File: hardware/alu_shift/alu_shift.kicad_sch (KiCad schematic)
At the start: 3 parts, among them J1 Conn_02x17_Odd_Even, U1 74HC00

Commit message: added LED indicators for ALU shift module
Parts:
- added D10, D11, D12, D13, D14, D15, D16, D17, D18, D19, D20, D21, D22, D23, D24, D25, D26, D27, D28, D8, D9: LED, LED_SMD:LED_0603_1608Metric_Pad1.05x0.95mm_HandSolder, symbol Device:LED
- added Q15, Q16, Q17, Q18, Q19, Q20, Q21, Q22, Q23, Q24, Q25, Q26, Q27, Q28, Q29, Q30, Q31, Q32, Q33, Q34, Q35: IRLML6244, Package_TO_SOT_SMD:SOT-23_Handsoldering, symbol Transistor_FET:IRLML6244
- added R22, R23, R24, R25, R26, R27, R28, R29, R30, R31, R32, R33, R34, R35, R36, R37, R38, R39, R40, R41, R42: 1000, Resistor_SMD:R_0603_1608Metric_Pad0.98x0.95mm_HandSolder, symbol Device:R
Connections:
- net +5V: now also Q15.3 (D), Q16.3 (D), Q17.3 (D), Q18.3 (D), Q19.3 (D), Q20.3 (D), Q21.3 (D), Q22.3 (D), Q23.3 (D), Q24.3 (D), Q25.3 (D), Q26.3 (D), Q27.3 (D), Q28.3 (D), Q29.3 (D), Q30.3 (D), Q31.3 (D), Q32.3 (D), Q33.3 (D), Q34.3 (D), Q35.3 (D)
- net A0: now also Q15.1 (G)
- net A1: now also Q16.1 (G)
- net A2: now also Q17.1 (G)
- net A3: now also Q18.1 (G)
- net A4: now also Q19.1 (G)
- net A5: now also Q20.1 (G)
- net A6: now also Q21.1 (G)
- net A7: now also Q22.1 (G)
- net BY0: now also Q31.1 (G)
- net BY1: now also Q32.1 (G)
- net BY2: now also Q33.1 (G)
- net DIR: now also Q35.1 (G); no longer U1.10, U1.4, U1.9
- net GND: now also R22.2, R23.2, R24.2, R25.2, R26.2, R27.2, R28.2, R29.2, R30.2, R31.2, R32.2, R33.2, R34.2, R35.2, R36.2, R37.2, R38.2, R39.2, R40.2, R41.2, R42.2
- net RES0: now also D16.2 (A), Q23.2 (S)
- net RES1: now also D17.2 (A), Q24.2 (S)
- net RES2: now also D18.2 (A), Q25.2 (S)
- net RES3: now also D19.2 (A), Q26.2 (S)
- net RES4: now also D20.2 (A), Q27.2 (S)
- net RES5: now also D21.2 (A), Q28.2 (S)
- net RES6: now also D22.2 (A), Q29.2 (S)
- net RES7: now also D23.2 (A), Q30.2 (S)
- net SOB: now also D27.2 (A), Q34.2 (S); no longer U1.11
- new net: D12.1 (K), R26.1
- new net: D11.1 (K), R25.1
- new net: D17.1 (K), R31.1
- new net: D8.1 (K), R22.1
- new net: D20.1 (K), R34.1
- new net: D19.1 (K), R33.1
- new net: D23.1 (K), R37.1
- new net: D25.1 (K), R39.1
- new net: Q34.1 (G), U1.11
- new net: D13.1 (K), R27.1
- new net: D27.1 (K), R41.1
- new net: D22.1 (K), R36.1
- new net: D15.1 (K), R29.1
- new net: D24.1 (K), R38.1
- new net: D28.1 (K), R42.1
- new net: D16.1 (K), R30.1
- new net: D10.1 (K), R24.1
- new net: D14.1 (K), R28.1
- new net: D21.1 (K), R35.1
- new net: D18.1 (K), R32.1
- new net: D9.1 (K), R23.1
- new net: D26.1 (K), R40.1
- new net MuxDirection/OUT0: Q23.1 (G)
- new net MuxDirection/OUT1: Q24.1 (G)
- new net MuxDirection/OUT2: Q25.1 (G)
- new net MuxDirection/OUT3: Q26.1 (G)
- new net MuxDirection/OUT4: Q27.1 (G)
- new net MuxDirection/OUT5: Q28.1 (G)
- new net MuxDirection/OUT6: Q29.1 (G)
- new net MuxDirection/OUT7: Q30.1 (G)
- new net MuxDirection/SEL: D28.2 (A), Q35.2 (S), U1.10, U1.4, U1.9
- new net MuxLeft1/A0: D8.2 (A), Q15.2 (S)
- new net MuxLeft1/A1: D9.2 (A), Q16.2 (S)
- new net MuxLeft1/A2: D10.2 (A), Q17.2 (S)
- new net MuxLeft1/A3: D11.2 (A), Q18.2 (S)
- new net MuxLeft1/A4: D12.2 (A), Q19.2 (S)
- new net MuxLeft1/A5: D13.2 (A), Q20.2 (S)
- new net MuxLeft1/A6: D14.2 (A), Q21.2 (S)
- new net MuxLeft1/A7: D15.2 (A), Q22.2 (S)
- new net MuxLeft1/SEL: D24.2 (A), Q31.2 (S)
- new net MuxLeft2/SEL: D25.2 (A), Q32.2 (S)
- new net MuxLeft4/SEL: D26.2 (A), Q33.2 (S)
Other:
- moved on the sheet: U1A, U1B, U1C, U1D

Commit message: added 8 bit mux pcb, started work on ALU shifter
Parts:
- Q1: renamed from Q15; footprint Package_TO_SOT_SMD:SOT-23_Handsoldering -> Package_TO_SOT_SMD:SOT-23-3
- Q10: renamed from Q31; footprint Package_TO_SOT_SMD:SOT-23_Handsoldering -> Package_TO_SOT_SMD:SOT-23-3
- Q11: renamed from Q35; footprint Package_TO_SOT_SMD:SOT-23_Handsoldering -> Package_TO_SOT_SMD:SOT-23-3
- Q12: renamed from Q32; footprint Package_TO_SOT_SMD:SOT-23_Handsoldering -> Package_TO_SOT_SMD:SOT-23-3
- Q13: renamed from Q33; footprint Package_TO_SOT_SMD:SOT-23_Handsoldering -> Package_TO_SOT_SMD:SOT-23-3
- Q14: renamed from Q23; footprint Package_TO_SOT_SMD:SOT-23_Handsoldering -> Package_TO_SOT_SMD:SOT-23-3
- Q15: renamed from Q24; footprint Package_TO_SOT_SMD:SOT-23_Handsoldering -> Package_TO_SOT_SMD:SOT-23-3
- Q16: renamed from Q25; footprint Package_TO_SOT_SMD:SOT-23_Handsoldering -> Package_TO_SOT_SMD:SOT-23-3
- Q17: renamed from Q26; footprint Package_TO_SOT_SMD:SOT-23_Handsoldering -> Package_TO_SOT_SMD:SOT-23-3
- Q18: renamed from Q27; footprint Package_TO_SOT_SMD:SOT-23_Handsoldering -> Package_TO_SOT_SMD:SOT-23-3
- Q19: renamed from Q28; footprint Package_TO_SOT_SMD:SOT-23_Handsoldering -> Package_TO_SOT_SMD:SOT-23-3
- Q2: renamed from Q16; footprint Package_TO_SOT_SMD:SOT-23_Handsoldering -> Package_TO_SOT_SMD:SOT-23-3
- Q20: renamed from Q29; footprint Package_TO_SOT_SMD:SOT-23_Handsoldering -> Package_TO_SOT_SMD:SOT-23-3
- Q21: renamed from Q30; footprint Package_TO_SOT_SMD:SOT-23_Handsoldering -> Package_TO_SOT_SMD:SOT-23-3
- Q3: renamed from Q17; footprint Package_TO_SOT_SMD:SOT-23_Handsoldering -> Package_TO_SOT_SMD:SOT-23-3
- Q4: renamed from Q18; footprint Package_TO_SOT_SMD:SOT-23_Handsoldering -> Package_TO_SOT_SMD:SOT-23-3
- Q5: renamed from Q19; footprint Package_TO_SOT_SMD:SOT-23_Handsoldering -> Package_TO_SOT_SMD:SOT-23-3
- Q6: renamed from Q20; footprint Package_TO_SOT_SMD:SOT-23_Handsoldering -> Package_TO_SOT_SMD:SOT-23-3
- Q7: renamed from Q21; footprint Package_TO_SOT_SMD:SOT-23_Handsoldering -> Package_TO_SOT_SMD:SOT-23-3
- Q8: renamed from Q22; footprint Package_TO_SOT_SMD:SOT-23_Handsoldering -> Package_TO_SOT_SMD:SOT-23-3
- Q9: renamed from Q34; footprint Package_TO_SOT_SMD:SOT-23_Handsoldering -> Package_TO_SOT_SMD:SOT-23-3
- renumbered D8 to D1, D24 to D10, D28 to D11, D25 to D12, D26 to D13, D16 to D14, D17 to D15, D18 to D16, D19 to D17, D20 to D18, D21 to D19, D9 to D2, D22 to D20, D23 to D21, D10 to D3, D11 to D4, D12 to D5, D13 to D6, D14 to D7, D15 to D8, D27 to D9, R22 to R1, R38 to R10, R42 to R11, R39 to R12, R40 to R13, R30 to R14, R31 to R15, R32 to R16, R33 to R17, R34 to R18, R35 to R19, R23 to R2, R36 to R20, R37 to R21, R24 to R3, R25 to R4, R26 to R5, R27 to R6, R28 to R7, R29 to R8, R41 to R9
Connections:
- net MuxDirection/OUT0 renamed MuxResult/RES0
- net MuxDirection/OUT1 renamed MuxResult/RES1
- net MuxDirection/OUT2 renamed MuxResult/RES2
- net MuxDirection/OUT3 renamed MuxResult/RES3
- net MuxDirection/OUT4 renamed MuxResult/RES4
- net MuxDirection/OUT5 renamed MuxResult/RES5
- net MuxDirection/OUT6 renamed MuxResult/RES6
- net MuxDirection/OUT7 renamed MuxResult/RES7
- net MuxDirection/SEL renamed MuxResult/SEL
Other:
- removed sheet MuxDirection
- added sheet MuxResult (mux.kicad_sch)
- sheet MuxLeft1 ports: added RES0, RES1, RES2, RES3, RES4, RES5, RES6, RES7; removed OUT0, OUT1, OUT2, OUT3, OUT4, OUT5, OUT6, OUT7
- sheet MuxLeft2 ports: added RES0, RES1, RES2, RES3, RES4, RES5, RES6, RES7; removed OUT0, OUT1, OUT2, OUT3, OUT4, OUT5, OUT6, OUT7
- sheet MuxLeft4 ports: added RES0, RES1, RES2, RES3, RES4, RES5, RES6, RES7; removed OUT0, OUT1, OUT2, OUT3, OUT4, OUT5, OUT6, OUT7
- sheet MuxRight1 ports: added RES0, RES1, RES2, RES3, RES4, RES5, RES6, RES7; removed OUT0, OUT1, OUT2, OUT3, OUT4, OUT5, OUT6, OUT7
- sheet MuxRight2 ports: added RES0, RES1, RES2, RES3, RES4, RES5, RES6, RES7; removed OUT0, OUT1, OUT2, OUT3, OUT4, OUT5, OUT6, OUT7
- sheet MuxRight4 ports: added RES0, RES1, RES2, RES3, RES4, RES5, RES6, RES7; removed OUT0, OUT1, OUT2, OUT3, OUT4, OUT5, OUT6, OUT7

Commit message: finished ALU Shift module, all ALU modules completed
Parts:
- added C12, C2, C3: 10uF, Capacitor_SMD:C_0603_1608Metric_Pad1.08x0.95mm_HandSolder, symbol Device:C
- added H1, H2, H3, H4: MountingHole_Pad, MountingHole:MountingHole_2.2mm_M2_Pad, symbol Mechanical:MountingHole_Pad
- added TP1, TP10, TP11, TP12, TP13, TP14, TP15, TP16, TP17, TP18, TP19, TP2, TP20, TP21, TP22, TP23, TP24, TP25, TP26, TP27, TP28, TP29, TP3, TP30, TP31, TP32, TP33, TP34, TP35, TP36, TP37, TP38, TP39, TP4, TP40, TP41, TP42, TP43, TP44, TP45, TP46, TP47, TP48, TP49, TP5, TP50, TP6, TP7, TP8, TP9: TestPoint, TestPoint:TestPoint_Pad_D2.0mm, symbol Connector:TestPoint
- J1: now not fitted; now left out of the parts list
- U1: LCSC (none) -> C5586
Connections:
- net +5V: now also C12.1, C2.1, C3.1
- net GND: now also C12.2, C2.2, C3.2, H1.1, H2.1, H3.1, H4.1
- net MuxLeft1/RES0: now also TP1.1
- net MuxLeft1/RES1: now also TP2.1
- net MuxLeft1/RES2: now also TP3.1
- net MuxLeft1/RES3: now also TP4.1
- net MuxLeft1/RES4: now also TP5.1
- net MuxLeft1/RES5: now also TP6.1
- net MuxLeft1/RES6: now also TP7.1
- net MuxLeft1/RES7: now also TP8.1
- net MuxLeft2/RES0: now also TP9.1
- net MuxLeft2/RES1: now also TP10.1
- net MuxLeft2/RES2: now also TP11.1
- net MuxLeft2/RES3: now also TP12.1
- net MuxLeft2/RES4: now also TP13.1
- net MuxLeft2/RES5: now also TP14.1
- net MuxLeft2/RES6: now also TP15.1
- net MuxLeft2/RES7: now also TP16.1
- net MuxLeft4/RES0: now also TP17.1
- net MuxLeft4/RES1: now also TP18.1
- net MuxLeft4/RES2: now also TP19.1
- net MuxLeft4/RES3: now also TP20.1
- net MuxLeft4/RES4: now also TP21.1
- net MuxLeft4/RES5: now also TP22.1
- net MuxLeft4/RES6: now also TP23.1
- net MuxLeft4/RES7: now also TP24.1
- net MuxResult/B0: now also TP41.1
- net MuxResult/B1: now also TP42.1
- net MuxResult/B2: now also TP43.1
- net MuxResult/B3: now also TP44.1
- net MuxResult/B4: now also TP45.1
- net MuxResult/B5: now also TP46.1
- net MuxResult/B6: now also TP47.1
- net MuxResult/B7: now also TP48.1
- net MuxRight1/RES0: now also TP25.1
- net MuxRight1/RES1: now also TP26.1
- net MuxRight1/RES2: now also TP27.1
- net MuxRight1/RES3: now also TP28.1
- net MuxRight1/RES4: now also TP29.1
- net MuxRight1/RES5: now also TP30.1
- net MuxRight1/RES6: now also TP31.1
- net MuxRight1/RES7: now also TP32.1
- net MuxRight2/RES0: now also TP33.1
- net MuxRight2/RES1: now also TP34.1
- net MuxRight2/RES2: now also TP35.1
- net MuxRight2/RES3: now also TP36.1
- net MuxRight2/RES4: now also TP37.1
- net MuxRight2/RES5: now also TP38.1
- net MuxRight2/RES6: now also TP39.1
- net MuxRight2/RES7: now also TP40.1
- net at U1.12, U1.3: now also TP49.1
- net at U1.13, U1.6: now also TP50.1

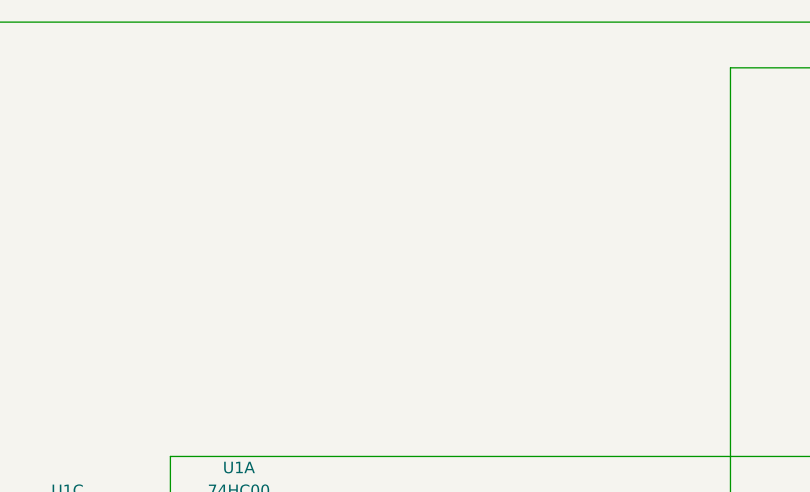
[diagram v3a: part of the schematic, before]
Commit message: added PWR indicator to alu_shift
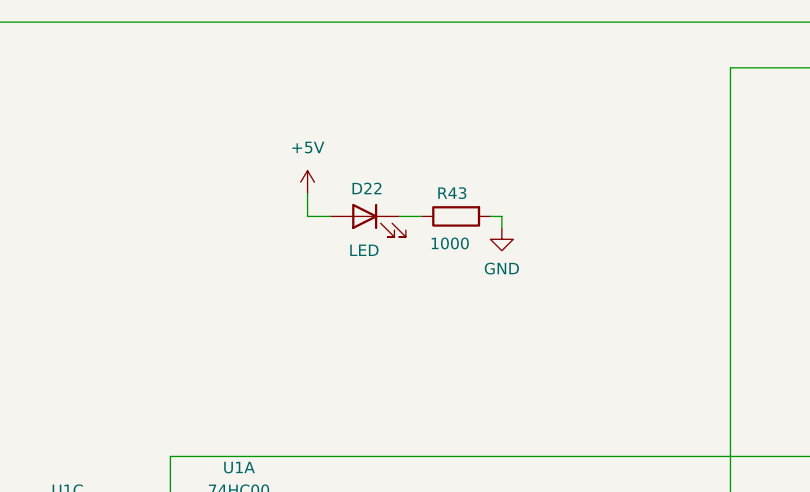
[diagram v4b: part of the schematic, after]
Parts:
- added D22: LED, LED_SMD:LED_0603_1608Metric_Pad1.05x0.95mm_HandSolder, symbol Device:LED
- added R43: 1000, Resistor_SMD:R_0603_1608Metric_Pad0.98x0.95mm_HandSolder, symbol Device:R
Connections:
- net +5V: now also D22.2 (A)
- net GND: now also R43.2
- new net: D22.1 (K), R43.1

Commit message: ALU shifter, bitops and motherboard as ordered
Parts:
- added D23: LED, LED_SMD:LED_0603_1608Metric_Pad1.05x0.95mm_HandSolder, symbol Device:LED
- added Q36: IRLML6244, Package_TO_SOT_SMD:SOT-23-3, symbol Transistor_FET:IRLML6244
- added R44: 1000, Resistor_SMD:R_0603_1608Metric_Pad0.98x0.95mm_HandSolder, symbol Device:R
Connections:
- net +5V: now also Q36.3 (D); no longer J1.24 (Pin_24)
- net GND: now also R44.2
- new net: D23.1 (K), R44.1
- new net MuxLeft1/B0: D23.2 (A), Q36.2 (S)
- new net SIB: J1.24 (Pin_24), Q36.1 (G)
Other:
- moved on the sheet: D22, R43
